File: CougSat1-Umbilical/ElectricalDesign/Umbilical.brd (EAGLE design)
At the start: 58.3 x 59.1 mm, 42 parts, among them J3 5V input, Q1 CSD16406Q3, Q2 CSD16406Q3, U1 FT230XQ, U2 BQ24650

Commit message: added test points
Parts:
- added TP1, TP2, TP3, TP4, TP5, TP6, TP7: TEST_POINT-THT-1.0, CougsInSpace-Connectors:THT-1.0
- moved C10 69.1 mm to (20.5, 30.7)
- moved R4 58.6 mm to (25.2, 47.6)
- moved C9 55.0 mm to (16.3, 53.7)
- moved R10 42.2 mm to (3.28, 40.5)
- moved R11 40.8 mm to (8.47, 41.5)
- moved C14 40.4 mm to (-2.59, 39.6)
- moved DS1 35.2 mm to (16.3, 51.6), turned to 180 degrees
- moved DS2 34.0 mm to (16.5, 42.6)
- moved R9 33.4 mm to (2.09, 46.5)
- moved C13 33.3 mm to (-2.91, 43.7)
- moved R3 33.0 mm to (-4.86, 28.5)
- moved R5 32.0 mm to (16.3, 45.5)
- moved R6 32.0 mm to (16.5, 48.5)
- moved R12 31.3 mm to (8.26, 44.5)
- moved C3 29.5 mm to (-2.72, 36.6), turned to 180.9 degrees
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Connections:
- net 5.0V: now also TP1.1
- net BAT_CHARGE_OUT: now also TP4.1
- net DIODE_OUT: now also TP2.1
- net PH: now also TP3.1
- net USB5V: now also TP5.1
- net USB5V_FILTERED: now also TP6.1
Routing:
- net 5.0V: track 30.2 -> 105.8 mm, vias 2 -> 4
- net SR_P: track 0.02 -> 71.7 mm, vias 0 -> 8
- net BAT_CHARGE_OUT: track 22.1 -> 84.8 mm, vias 2 -> 3
- net VFB: track 14.4 -> 76.5 mm, vias 2 -> 4
- net TS: track 16.2 -> 67.8 mm, vias 0 -> 4
- net PGND: track 154.4 -> 200.3 mm, vias 2 -> 4
- net CHARGING_STAT_G: track 0.00 -> 41.5 mm, vias 0 -> 4
- net CHARGING_STAT_R: track 0.00 -> 39.7 mm, vias 0 -> 2
- net VCC: track 0.00 -> 38.2 mm, vias 0 -> 4
- net VREF: track 0.88 -> 38.4 mm, vias 0 -> 2
- net DIODE_OUT: track 15.0 -> 50.7 mm, vias 2 -> 4
- net USB_CONN_P: track 0.00 -> 31.9 mm, vias 0 -> 2
- net USB_N: track 16.4 -> 39.7 mm, vias 1 -> 2
- net BTST: track 23.9 -> 42.5 mm, vias 1 -> 4
- net PH: track 34.5 -> 49.0 mm, vias 4 -> 5
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
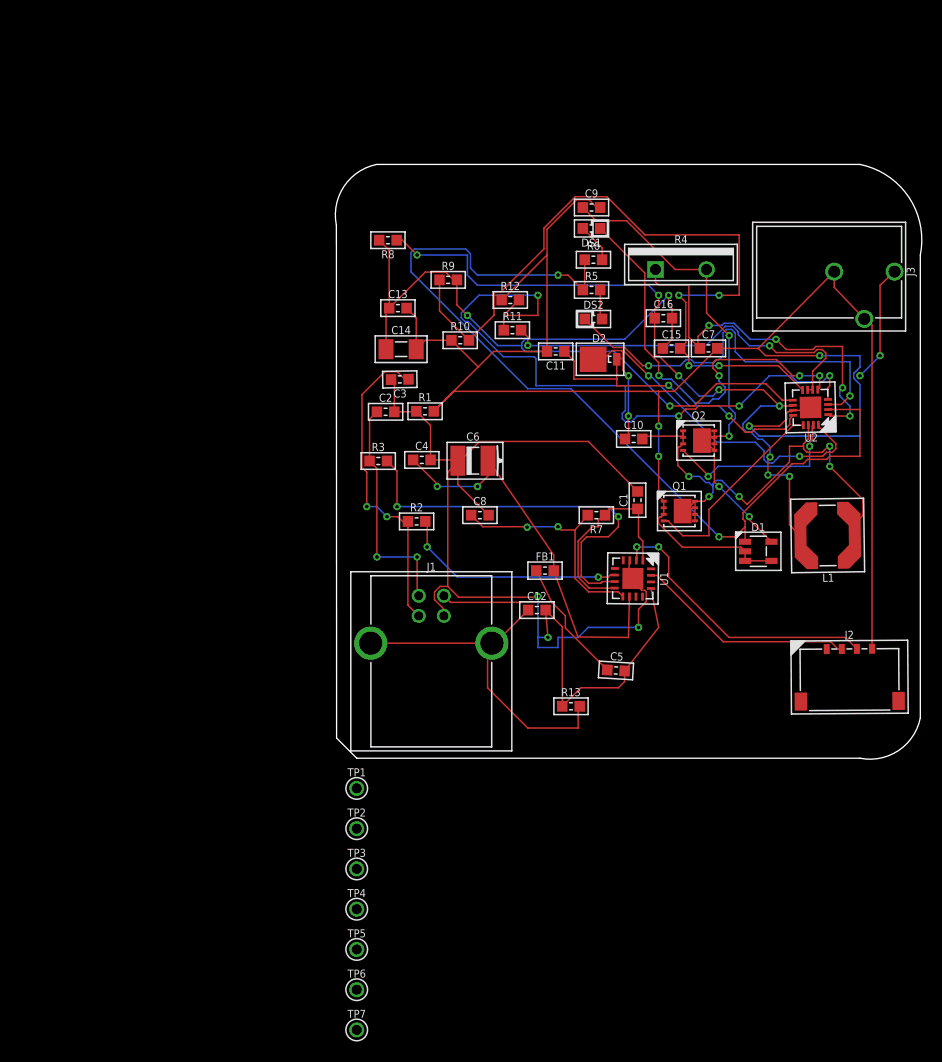
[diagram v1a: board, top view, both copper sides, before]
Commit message: fixed board outline
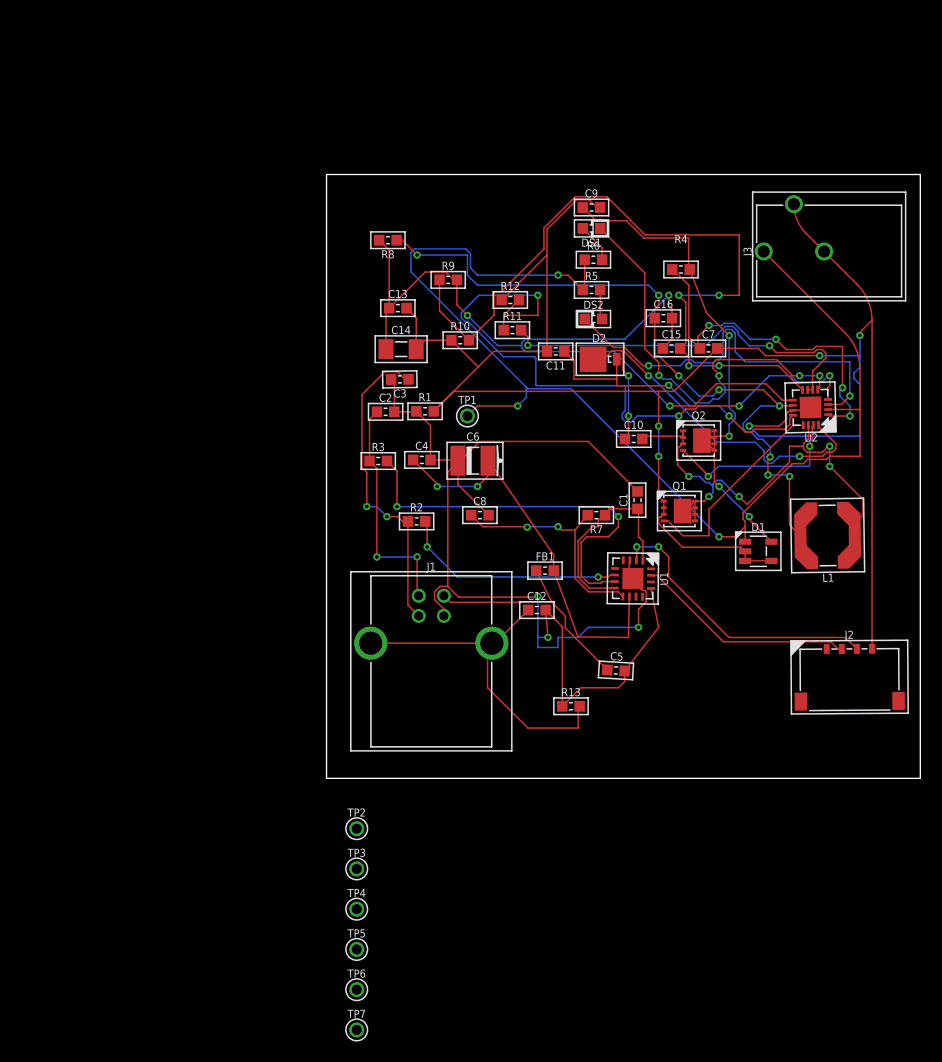
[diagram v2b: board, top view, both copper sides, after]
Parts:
- R4: device CougsInSpace-Resistors:TO-220-2 -> CougsInSpace-Resistors:1608
- moved TP1 38.6 mm to (4.00, 33.0)
- moved J3 7.28 mm to (36.4, 49.4), turned to 270 degrees
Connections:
- net DIODE_OUT: now also R4.2; no longer R4.3
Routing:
- net 5.0V: track 105.8 -> 120.9 mm, vias 4 -> 3
- net VCC: track 38.2 -> 35.8 mm
- net DIODE_OUT: track 50.7 -> 51.6 mm
- net PGND: track 200.3 -> 200.7 mm, vias 4 -> 5
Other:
- board size 58.3 x 59.1 mm -> 59 x 60 mm

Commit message: Placed components
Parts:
- removed TP7: TEST_POINT-THT-1.0, CougsInSpace-Connectors:THT-1.0
- J1: value (none) -> USB
- J2: value (none) -> Umbilical
- moved TP4 66.3 mm to (33.4, 36.6)
- moved TP6 48.4 mm to (6.00, 22.6)
- moved TP3 44.9 mm to (27.3, 16.9)
- moved TP2 44.3 mm to (29.6, 16.9)
- moved J3 40.6 mm to (31.9, 9.00), turned to 180 degrees
- moved R8 39.4 mm to (30.2, 30.8), turned to 0 degrees
- moved C13 39.1 mm to (34.7, 33.1)
- moved C9 38.5 mm to (34.6, 19.8), turned to 270 degrees
- moved TP5 37.7 mm to (1.10, 16.8)
- moved C14 37.5 mm to (33.5, 29.5), turned to 270 degrees
- moved J2 32.4 mm to (23.7, 36.6), turned to 90 degrees
- moved TP1 31.6 mm to (29.6, 14.4)
- moved R9 30.5 mm to (30.2, 34.6)
- moved U1 25.1 mm to (-3.70, 23.7), turned to 0 degrees
- moved DS1 24.2 mm to (12.1, 27.8)
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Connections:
- net N$1 renamed USB_RESET
- removed net BAT_CHARGE_OUT: C13.1, C14.1, C15.1, C16.2, R8.2, R9.2, TP4.1, U2.9
- net UMB_IN: now also C13.1, C14.1, C15.1, C16.2, R8.2, R9.2, TP4.1, U2.9
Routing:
- net PGND: track 200.7 -> 0.00 mm, vias 5 -> 0
- net DGND: track 125.4 -> 0.00 mm, vias 3 -> 0
- net 5.0V: track 120.9 -> 0.00 mm, vias 3 -> 0
- net BAT_CHARGE_OUT: track 84.8 -> 0.00 mm, vias 3 -> 0
- net VFB: track 76.5 -> 0.00 mm, vias 4 -> 0
- net SR_P: track 71.7 -> 0.00 mm, vias 8 -> 0
- net TS: track 67.8 -> 0.00 mm, vias 4 -> 0
- net DIODE_OUT: track 51.6 -> 0.00 mm, vias 4 -> 0
- net PH: track 49.0 -> 0.00 mm, vias 5 -> 0
- net BTST: track 42.5 -> 0.00 mm, vias 4 -> 0
- net CHARGING_STAT_G: track 41.5 -> 0.00 mm, vias 4 -> 0
- net USB_N: track 39.7 -> 0.00 mm, vias 2 -> 0
- net CHARGING_STAT_R: track 39.7 -> 0.00 mm, vias 2 -> 0
- net USB5V_FILTERED: track 39.5 -> 0.00 mm, vias 2 -> 0
- net VREF: track 38.4 -> 0.00 mm, vias 2 -> 0
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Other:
- board size 59 x 60 mm -> 49 x 48 mm

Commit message: Exported PDF
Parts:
- U1: device CougsInSpace-IC-Conversion:QFN-16-4040 -> CougsInSpace-IC-Comms:QFN-16-4040
- moved C5 3.00 mm to (7.10, 16.5)
- moved C9 2.00 mm to (36.6, 19.8)
- moved R1 1.36 mm to (3.10, 29.6)
- moved C6 1.32 mm to (3.00, 26.0)
- moved C4 1.10 mm to (-0.10, 25.2)
- moved C8 1.00 mm to (6.80, 20.4)
- moved Q2 1.00 mm to (32.4, 20.1)
- moved DS2 0.98 mm to (18.4, 29.5)
- moved D2 0.91 mm to (21.9, 18.1)
- moved C11 0.90 mm to (16.9, 18.2)
- moved R12 0.70 mm to (14.1, 25.1)
- moved TP5 0.67 mm to (1.70, 16.5)
- moved J2 0.60 mm to (23.7, 37.2)
- moved R11 0.60 mm to (16.0, 25.1)
- moved R5 0.51 mm to (15.7, 29.7)
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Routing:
- net PGND: track 0.00 -> 123.9 mm, vias 0 -> 4
- net DGND: track 0.00 -> 64.3 mm, vias 0 -> 4
- net 5.0V: track 0.00 -> 56.9 mm, vias 0 -> 2
- net UMB_IN: track 0.00 -> 47.8 mm, vias 0 -> 2
- net UMB_TX: track 0.00 -> 45.4 mm, vias 0 -> 2
- net UMB_RX: track 0.00 -> 37.7 mm
- net DIODE_OUT: track 0.00 -> 37.7 mm, vias 0 -> 2
- net PH: track 0.00 -> 24.6 mm, vias 0 -> 2
- net SR_P: track 0.00 -> 24.4 mm, vias 0 -> 2
- net VFB: track 0.00 -> 24.3 mm, vias 0 -> 2
- net BTST: track 0.00 -> 19.9 mm, vias 0 -> 2
- net 3.3V: track 0.00 -> 18.8 mm, vias 0 -> 2
- net CHASSIS: track 0.00 -> 17.8 mm
- net CHARGING_STAT_G: track 0.00 -> 13.3 mm, vias 0 -> 2
- net USB5V_FILTERED: track 0.00 -> 12.8 mm
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
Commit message: Fixed issues
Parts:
- removed C12: 100nF 10%, CougsInSpace-Capacitors:1608
- removed R13: 0Ω <20mΩ, CougsInSpace-Resistors:1608
- added R14: 0Ω <20mΩ, CougsInSpace-Resistors:1608
- moved C15 10.4 mm to (40.2, 39.5)
- moved C16 10.4 mm to (40.2, 35.7)
- moved J2 10.4 mm to (33.7, 40.2)
- moved R6 10.4 mm to (22.1, 32.7)
- moved R8 10.4 mm to (40.2, 33.8)
- moved R9 10.4 mm to (40.2, 37.6)
- moved C1 10.4 mm to (9.20, 22.2)
- moved C10 10.4 mm to (33.6, 24.8)
- moved C11 10.4 mm to (26.9, 21.2)
- moved C13 10.4 mm to (44.7, 36.1)
- moved C14 10.4 mm to (43.5, 32.5)
- moved C2 10.4 mm to (8.60, 19.5)
- moved C3 10.4 mm to (4.50, 19.1)
- moved C4 10.4 mm to (9.90, 28.2)
- moved C5 10.4 mm to (17.1, 19.5)
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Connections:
- net CHASSIS: now also R14.1; no longer C12.1, R13.2
- net DGND: no longer C12.2, R13.1
- net PGND: now also R14.2
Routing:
- net PGND: track 123.9 -> 133.4 mm
- net DGND: track 64.3 -> 56.0 mm
- net CHASSIS: track 17.8 -> 16.3 mm
- net UMB_IN: track 47.8 -> 46.6 mm
- net PH: track 24.6 -> 23.4 mm
- net DIODE_OUT: track 37.7 -> 36.8 mm
- added copper zone on layer 16, net BALANCING-BOTTOM
- added copper zone on layer 1, net BALANCING-TOP
- added copper zone on layer 16, net DGND
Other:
- board text added: "Umbilical V1.0 1915"

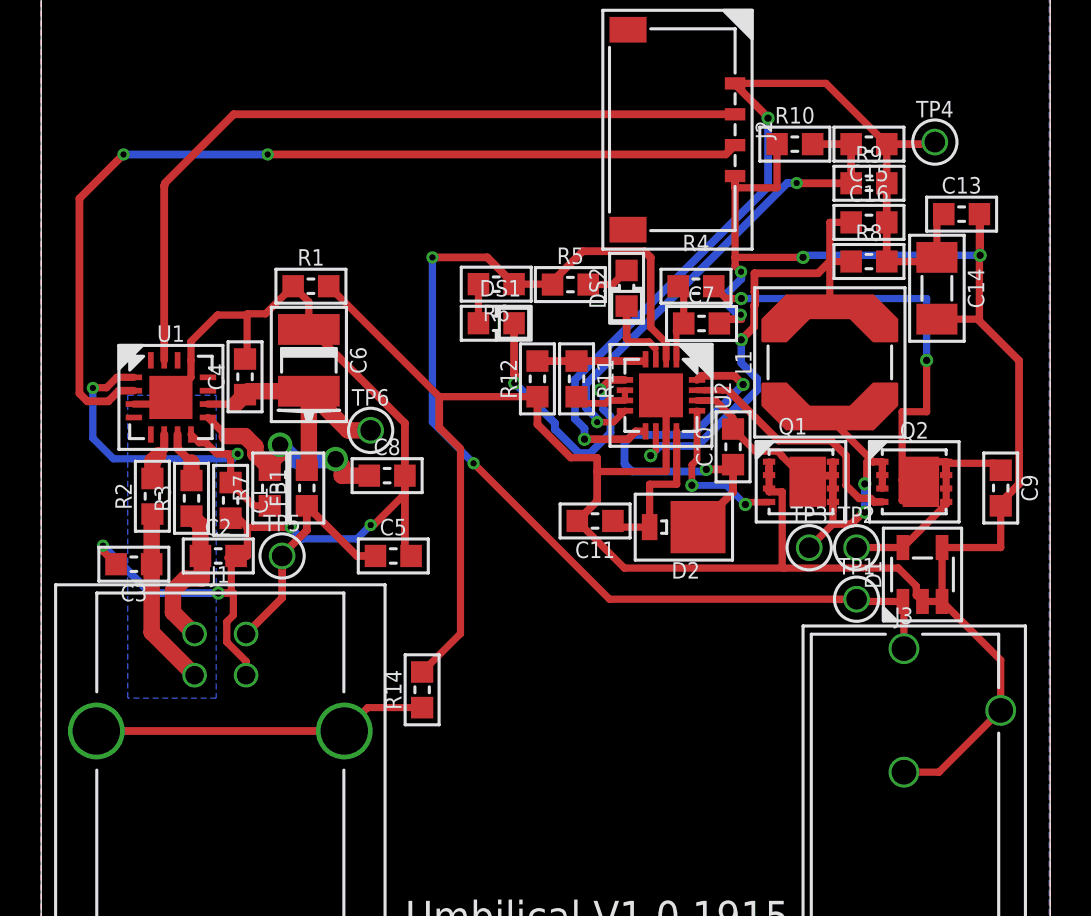
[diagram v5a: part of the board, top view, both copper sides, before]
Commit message: Fixed formatting
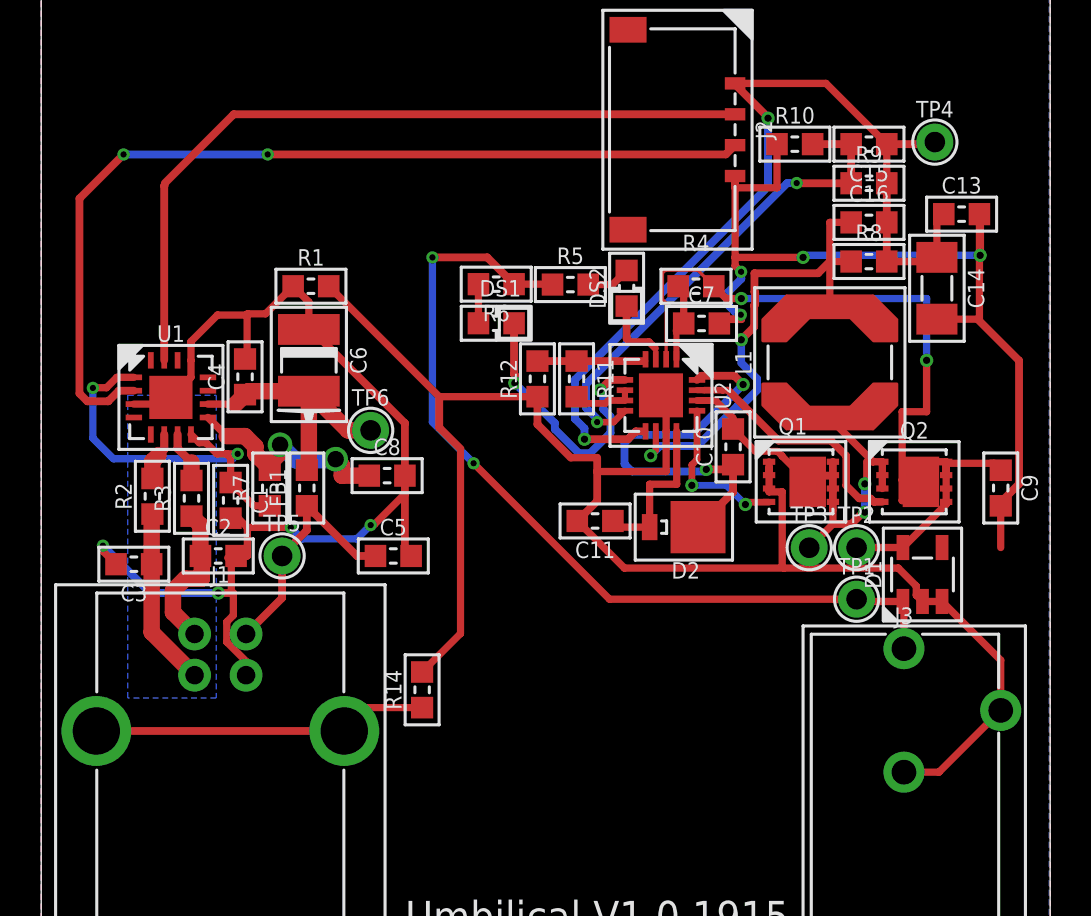
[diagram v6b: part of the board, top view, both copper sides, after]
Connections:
- net UMB_IN renamed UMB_OUT
- net 5.0V: no longer U2.2
- net DIODE_OUT: now also U2.2
- net PGND: no longer D1.4
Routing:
- net 5.0V: track 56.4 -> 45.5 mm
- net DIODE_OUT: track 36.8 -> 44.0 mm
- net PGND: track 133.4 -> 128.0 mm
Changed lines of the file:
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@@
 <?xml version="1.0" encoding="utf-8"?>
 <!DOCTYPE eagle SYSTEM "eagle.dtd">
-<eagle version="9.3.2">
+<eagle version="9.4.2">
 <drawing>
 <settings>
@@
 <setting verticaltext="up"/>
 </settings>
-<grid distance="0.1" unitdist="mm" unit="mm" style="lines" multiple="1" display="yes" altdistance="0.01" altunitdist="mm" altunit="mm"/>
+<grid distance="0.1" unitdist="mm" unit="mm" style="lines" multiple="1" display="yes" altdistance="0.005" altunitdist="mm" altunit="mm"/>
 <layers>
 <layer number="1" name="Top" color="4" fill="1" visible="yes" active="yes"/>
@@
 <contactref element="C14" pad="2"/>
 <contactref element="D1" pad="2"/>
-<contactref element="D1" pad="4"/>
 <contactref element="D1" pad="3"/>
 <contactref element="R10" pad="1"/>
@@
 <contactref element="J2" pad="4"/>
 <contactref element="R1" pad="2"/>
-<wire x1="43.75" y1="17.29" x2="43.75" y2="19.91" width="0.355" layer="1"/>
 <wire x1="42.8" y1="17.29" x2="43.75" y2="17.29" width="0.355" layer="1"/>
 <wire x1="43.75" y1="17.29" x2="46.6" y2="14.44" width="0.355" layer="1"/>
@@
 <via x="45.6" y="34.1" extent="1-16" drill="0.35"/>
 <wire x1="43.5" y1="31" x2="45.4775" y2="31" width="0.355" layer="1"/>
-<wire x1="43.75" y1="19.91" x2="46.6" y2="19.91" width="0.355" layer="1"/>
 <wire x1="46.6" y1="19.91" x2="46.6" y2="21.935" width="0.355" layer="1"/>
 <wire x1="45.565" y1="36.1" x2="45.565" y2="31" width="0.355" layer="1"/>
@@
 <wire x1="20.365" y1="24.7" x2="19.33" y2="25.735" width="0.38" layer="1"/>
 <wire x1="19.33" y1="25.735" x2="19.33" y2="27.235" width="0.38" layer="1"/>
+<wire x1="43.75" y1="17.29" x2="46.6" y2="19.91" width="0" layer="19" extent="1-1"/>
 </signal>
 <signal name="DIODE_OUT">
@@
 <wire x1="43.95" y1="23.425" x2="43.95" y2="22.7" width="0.16" layer="1"/>
 <wire x1="43.95" y1="22.775" x2="43.95" y2="22.7" width="0.355" layer="1"/>
+<contactref element="U2" pad="2"/>
+<wire x1="30.35" y1="29.05" x2="30.35" y2="31.7805875" width="0.16" layer="1"/>
+<wire x1="30.35" y1="31.7805875" x2="30.17" y2="31.9605875" width="0.16" layer="1"/>
+<wire x1="30.17" y1="33.2394125" x2="30.3105875" y2="33.38" width="0.16" layer="1"/>
+<wire x1="30.3105875" y1="33.38" x2="31.885" y2="33.38" width="0.16" layer="1"/>
+<wire x1="31.885" y1="33.38" x2="32.665" y2="32.6" width="0.16" layer="1"/>
+<wire x1="30.17" y1="31.9605875" x2="30.17" y2="33.2394125" width="0.16" layer="1"/>
 </signal>
 <signal name="BTST">
@@
 <contactref element="D1" pad="1"/>
 <contactref element="J3" pad="1"/>
-<contactref element="U2" pad="2"/>
 <contactref element="TP1" pad="1"/>
 <wire x1="41.9" y1="15" x2="41.9" y2="17.24" width="0.355" layer="1"/>
@@
 <via x="19" y="34" extent="1-16" drill="0.3"/>
 <wire x1="24.835" y1="32.68" x2="24.815" y2="32.7" width="0.355" layer="1"/>
-<wire x1="24.815" y1="32.7" x2="24.7" y2="32.7" width="0.355" layer="1"/>
-<wire x1="24.7" y1="32.7" x2="22.965" y2="32.7" width="0.355" layer="1"/>
+<wire x1="24.815" y1="32.7" x2="22.965" y2="32.7" width="0.355" layer="1"/>
 <wire x1="22.965" y1="32.7" x2="21.665" y2="34" width="0.38" layer="1"/>
 <wire x1="21.665" y1="34" x2="19" y2="34" width="0.38" layer="1"/>
-<wire x1="29.6" y1="34" x2="29.6" y2="30.6" width="0.38" layer="1"/>
-<wire x1="29.6" y1="34" x2="29.3" y2="34.3" width="0.38" layer="1"/>
-<wire x1="29.3" y1="34.3" x2="26.3" y2="34.3" width="0.38" layer="1"/>
-<wire x1="26.3" y1="34.3" x2="24.7" y2="32.7" width="0.38" layer="1"/>
 <wire x1="40.8" y1="17.29" x2="38.61" y2="17.29" width="0.16" layer="1"/>
 <wire x1="38.61" y1="17.29" x2="38.5" y2="17.4" width="0.16" layer="1"/>
-<wire x1="29.6" y1="30.6" x2="30.35" y2="29.85" width="0.35" layer="1"/>
-<wire x1="30.35" y1="29.85" x2="30.35" y2="29.05" width="0.35" layer="1"/>
 </signal>
 <signal name="CHARGING_STAT_G">
@@
 <wire x1="28.6" y1="29.9" x2="29.5137625" y2="29.9" width="0.35" layer="1"/>
 <wire x1="29.5137625" y1="29.9" x2="29.825" y2="29.5887625" width="0.35" layer="1"/>
-<wire x1="29.825" y1="29.5887625" x2="29.825" y2="29.075" width="0.16" layer="1"/>
-<wire x1="29.825" y1="29.075" x2="29.85" y2="29.05" width="0.16" layer="1"/>
+<wire x1="29.825" y1="29.5887625" x2="29.85" y2="29.5637625" width="0.16" layer="1"/>
+<wire x1="29.85" y1="29.5637625" x2="29.85" y2="29.05" width="0.16" layer="1"/>
 </signal>
 <signal name="VCC">
@@
 <wire x1="24.1" y1="28.965" x2="29.3" y2="28.965" width="0.38" layer="1"/>
 </signal>
-<signal name="UMB_IN">
+<signal name="UMB_OUT">
 <contactref element="J2" pad="1"/>
 <contactref element="U2" pad="9"/>

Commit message: Merged and fixed conflicts
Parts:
- added DS3: Green, CougsInSpace-LEDs:1608-POL
- added DS5: Red, CougsInSpace-LEDs:1608-POL
- added R13, R15: 1kΩ 0.1%, CougsInSpace-Resistors:1608
- added RN1: 10kΩ 1%, CougsInSpace-Resistors:1632
- moved R14 7.07 mm to (25.5, 14.0)
- moved R1 3.50 mm to (13.0, 36.1)
- moved C6 3.32 mm to (16.1, 30.2)
- moved J1 2.10 mm to (10.8, 11.1)
- moved C1 1.70 mm to (10.9, 22.3)
- moved C2 1.70 mm to (10.3, 19.6)
- moved TP5 1.70 mm to (13.4, 19.6)
- moved R7 1.70 mm to (12.8, 22.9)
- moved U1 1.70 mm to (8.00, 27.3)
- moved C3 1.70 mm to (6.20, 19.2)
- moved R3 1.70 mm to (9.00, 22.4)
- moved C4 1.70 mm to (11.6, 28.3)
- moved C5 1.70 mm to (18.8, 19.6)
- moved C8 1.70 mm to (18.5, 23.5)
- moved R2 1.70 mm to (7.10, 22.5)
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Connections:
- new net !CTS: RN1.4, U1.4
- new net !RTS: RN1.3, U1.16
- new net CBUS1: R15.1, U1.11
- new net CBUS2: R13.1, U1.5
- new net RXLED_C: DS5.C, R13.2
- new net TXLED_C: DS3.C, R15.2
- net 3.3V: now also DS3.A, DS5.A, RN1.5, RN1.6, RN1.7, RN1.8
- net UMB_RX: now also RN1.1
- net UMB_TX: now also RN1.2
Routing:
- net UMB_TX: track 45.4 -> 0.00 mm, vias 2 -> 0
- net UMB_RX: track 37.7 -> 0.04 mm
- net CBUS1: track 0.00 -> 16.2 mm, vias 0 -> 2
- net DGND: track 56.0 -> 71.9 mm
- net CBUS2: track 0.00 -> 9.30 mm, vias 0 -> 2
- net CHASSIS: track 16.3 -> 22.4 mm
- net PGND: track 128.0 -> 132.4 mm
- net TXLED_C: track 0.00 -> 3.47 mm
- net USB5V_FILTERED: track 12.8 -> 16.2 mm
- net RXLED_C: track 0.00 -> 2.08 mm
- net USB_RESET: track 11.1 -> 12.8 mm
- net 3.3V: track 18.7 -> 17.1 mm
- net 5.0V: track 45.5 -> 44.3 mm
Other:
- board text added: "Umbilical V1.0.3"
- board text removed: "Umbilical V1.0 1915"

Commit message: Updated Umbilical
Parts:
- moved RN1 50.3 mm to (10.1, 40.4), turned to 180 degrees
- moved DS5 40.8 mm to (6.30, 35.1), turned to 90 degrees
- moved DS3 27.6 mm to (2.30, 25.3)
- moved R15 7.30 mm to (2.00, 37.8)
- moved TP1 0.67 mm to (39.3, 16.8)
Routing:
- net UMB_TX: track 0.00 -> 51.3 mm, vias 0 -> 6
- net UMB_RX: track 0.04 -> 48.7 mm, vias 0 -> 2
- net 3.3V: track 17.1 -> 50.4 mm, vias 2 -> 4
- net !CTS: track 0.00 -> 20.4 mm, vias 0 -> 4
- net !RTS: track 0.00 -> 18.6 mm, vias 0 -> 2
- net RXLED_C: track 2.08 -> 17.4 mm
- net TXLED_C: track 3.47 -> 12.6 mm
- net CBUS1: track 16.2 -> 24.7 mm
- net PGND: track 132.4 -> 136.3 mm
- net UMB_OUT: track 46.6 -> 48.7 mm
- net CBUS2: track 9.30 -> 9.91 mm
